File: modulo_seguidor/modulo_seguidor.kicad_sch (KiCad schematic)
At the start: 12 parts, among them J1 Battery, J4 Motor Izquierdo, J5 Motor Derecho, J6 puerto sensores, SW1 SW_Push, U1 LM7806_TO220

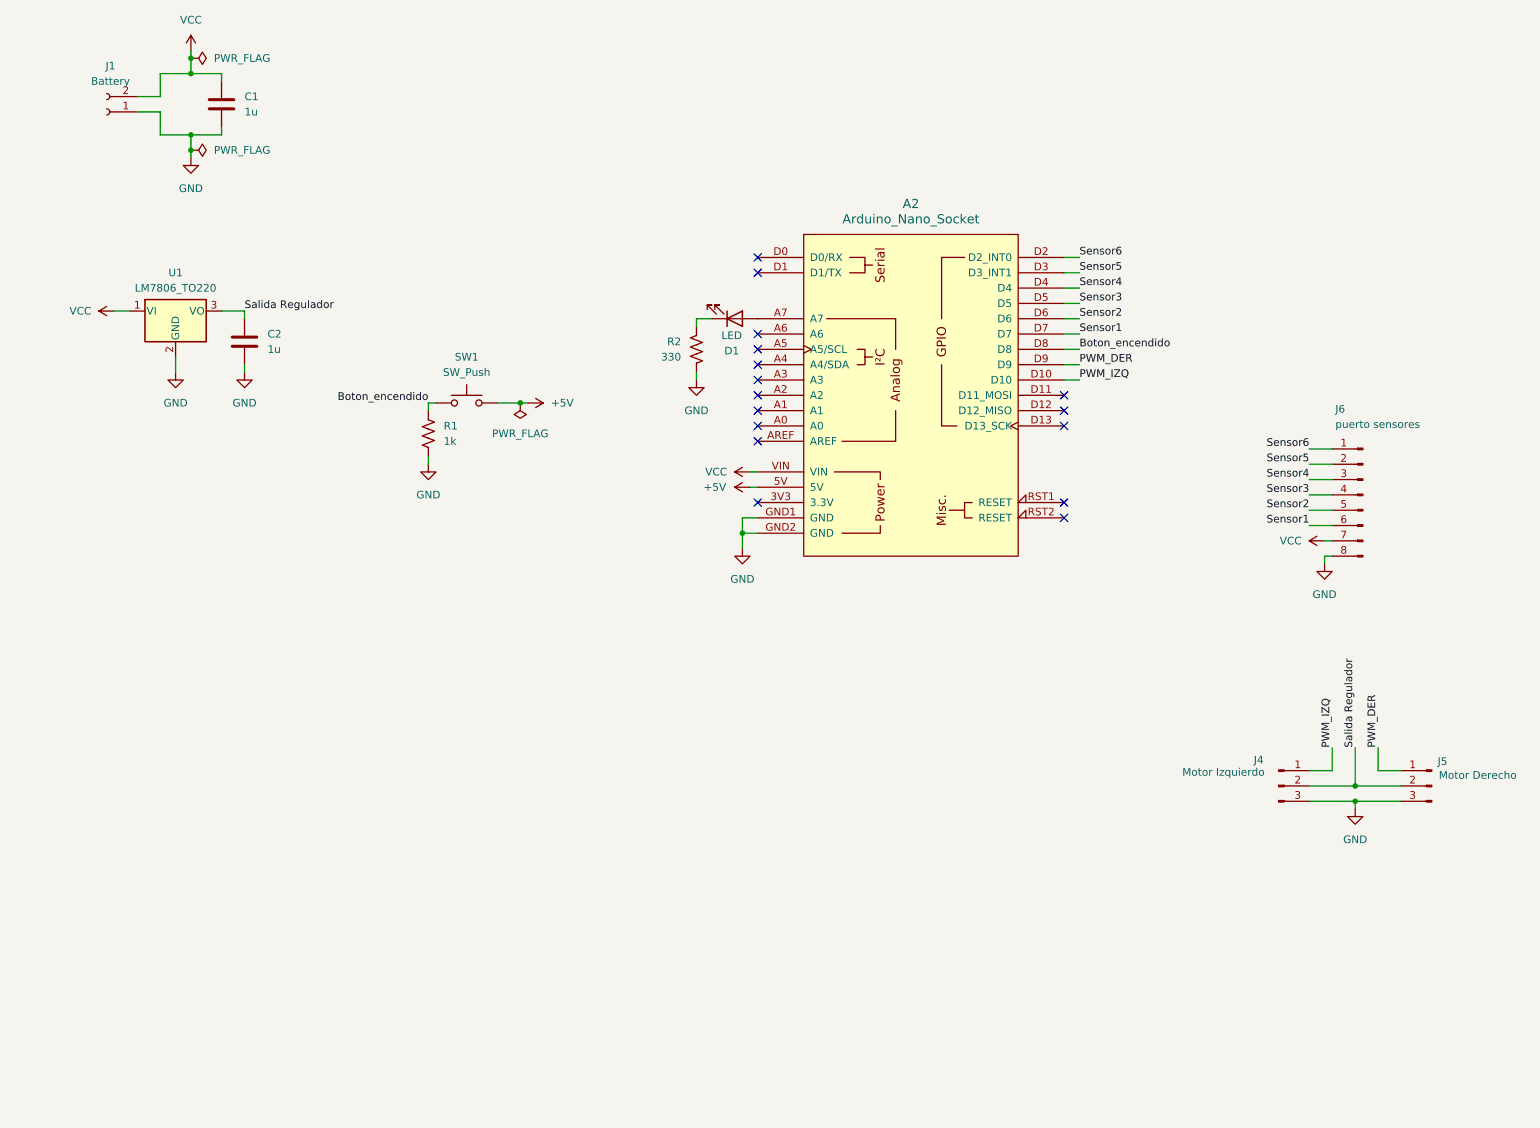
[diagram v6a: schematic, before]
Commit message: refactor(modulo_seguidor): Merge del seguidor y el puente H
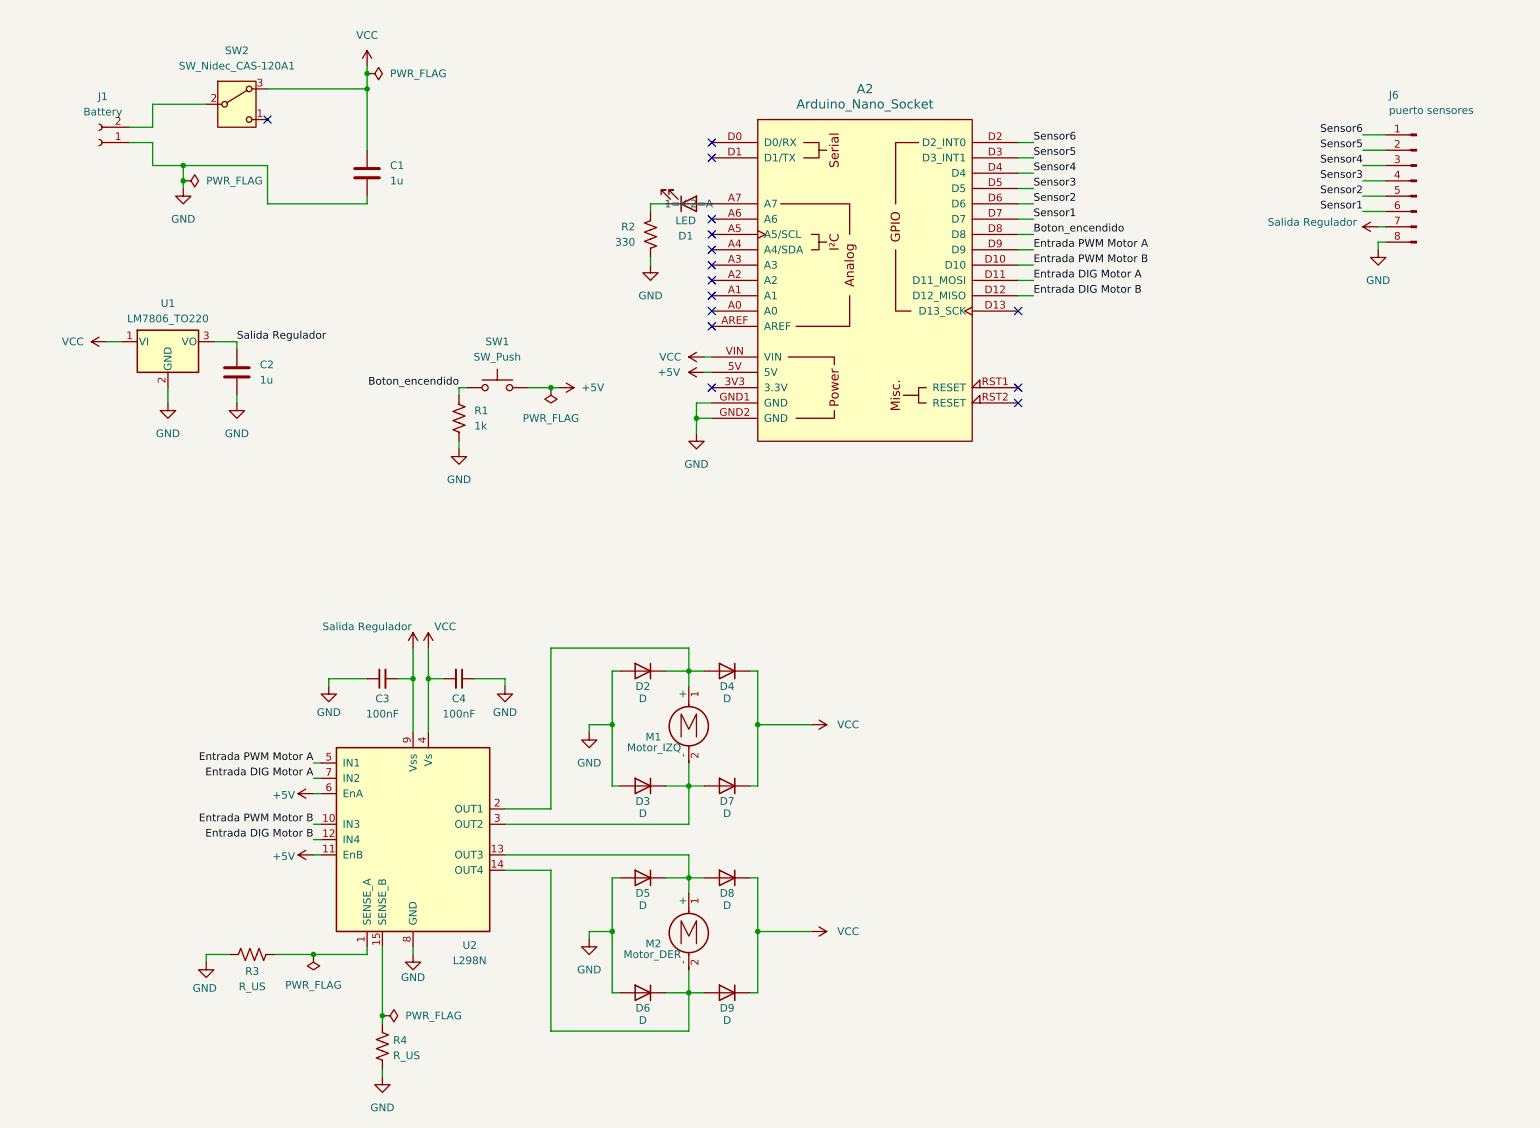
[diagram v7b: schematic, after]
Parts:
- removed J4: Motor Izquierdo, Connector_PinHeader_2.54mm:PinHeader_1x03_P2.54mm_Vertical, symbol Connector:Conn_01x03_Pin
- removed J5: Motor Derecho, Connector_PinHeader_2.54mm:PinHeader_1x03_P2.54mm_Vertical, symbol Connector:Conn_01x03_Pin
- added C3, C4: 100nF, Capacitor_THT:C_Disc_D7.0mm_W2.5mm_P5.00mm, symbol Device:C_Small
- added D2, D3, D4, D5, D6, D7, D8, D9: D, Diode_THT:D_DO-41_SOD81_P7.62mm_Horizontal, symbol Device:D
- added M1: Motor_IZQ, Resistor_THT:R_Axial_DIN0207_L6.3mm_D2.5mm_P2.54mm_Vertical, symbol Motor:Motor_DC
- added M2: Motor_DER, Resistor_THT:R_Axial_DIN0207_L6.3mm_D2.5mm_P2.54mm_Vertical, symbol Motor:Motor_DC
- added R3, R4: R_US, Resistor_SMD:R_0805_2012Metric_Pad1.20x1.40mm_HandSolder, symbol Device:R_US
- added SW2: SW_Nidec_CAS-120A1, Button_Switch_SMD:Nidec_Copal_CAS-120A, symbol Switch:SW_Nidec_CAS-120A1
- added U2: L298N, Package_TO_SOT_THT:TO-220-15_P2.54x5.08mm_StaggerOdd_Lead4.58mm_Vertical, symbol Driver_Motor:L298N
- A2: footprint PCM_arduino-library:Arduino_Nano_Socket -> Module:Arduino_Nano
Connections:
- net +5V: now also U2.11 (EnB), U2.6 (EnA)
- net GND: now also C3.1, C4.1, D2.2 (A), D3.2 (A), D5.2 (A), D6.2 (A), R3.2, R4.1, U2.8 (GND)
- net Salida Regulador: now also J6.7 (Pin_7), C3.2, U2.9 (Vss)
- net VCC: now also C4.2, D4.1 (K), D7.1 (K), D8.1 (K), D9.1 (K), SW2.3 (A), U2.4 (Vs); no longer J1.2 (Pin_2), J6.7 (Pin_7)
- net Entrada DIG Motor A: now reaches A2.D11 (D11_MOSI)
- net Entrada DIG Motor A: now also U2.7 (IN2)
- net Entrada DIG Motor B: now reaches A2.D12 (D12_MISO)
- net Entrada DIG Motor B: now also U2.12 (IN4)
- net PWM_DER renamed Entrada PWM Motor A
- net Entrada PWM Motor A: now also U2.5 (IN1)
- net PWM_IZQ renamed Entrada PWM Motor B
- net Entrada PWM Motor B: now also U2.10 (IN3)
- new net: R3.1, U2.1 (SENSE_A)
- new net: D3.1 (K), D7.2 (A), M1.2 (-), U2.3 (OUT2)
- new net: D5.1 (K), D8.2 (A), M2.1 (+), U2.13 (OUT3)
- new net: D6.1 (K), D9.2 (A), M2.2 (-), U2.14 (OUT4)
- new net: D2.1 (K), D4.2 (A), M1.1 (+), U2.2 (OUT1)
- new net: R4.2, U2.15 (SENSE_B)
- new net: J1.2 (Pin_2), SW2.2 (B)
- no-connect marks 16 -> 15
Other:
- moved on the sheet: A2, C1, C2, D1, J1, J6, R1, R2, SW1, U1

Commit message: feat(seguidor): Corrijo errores de DRC esquemático
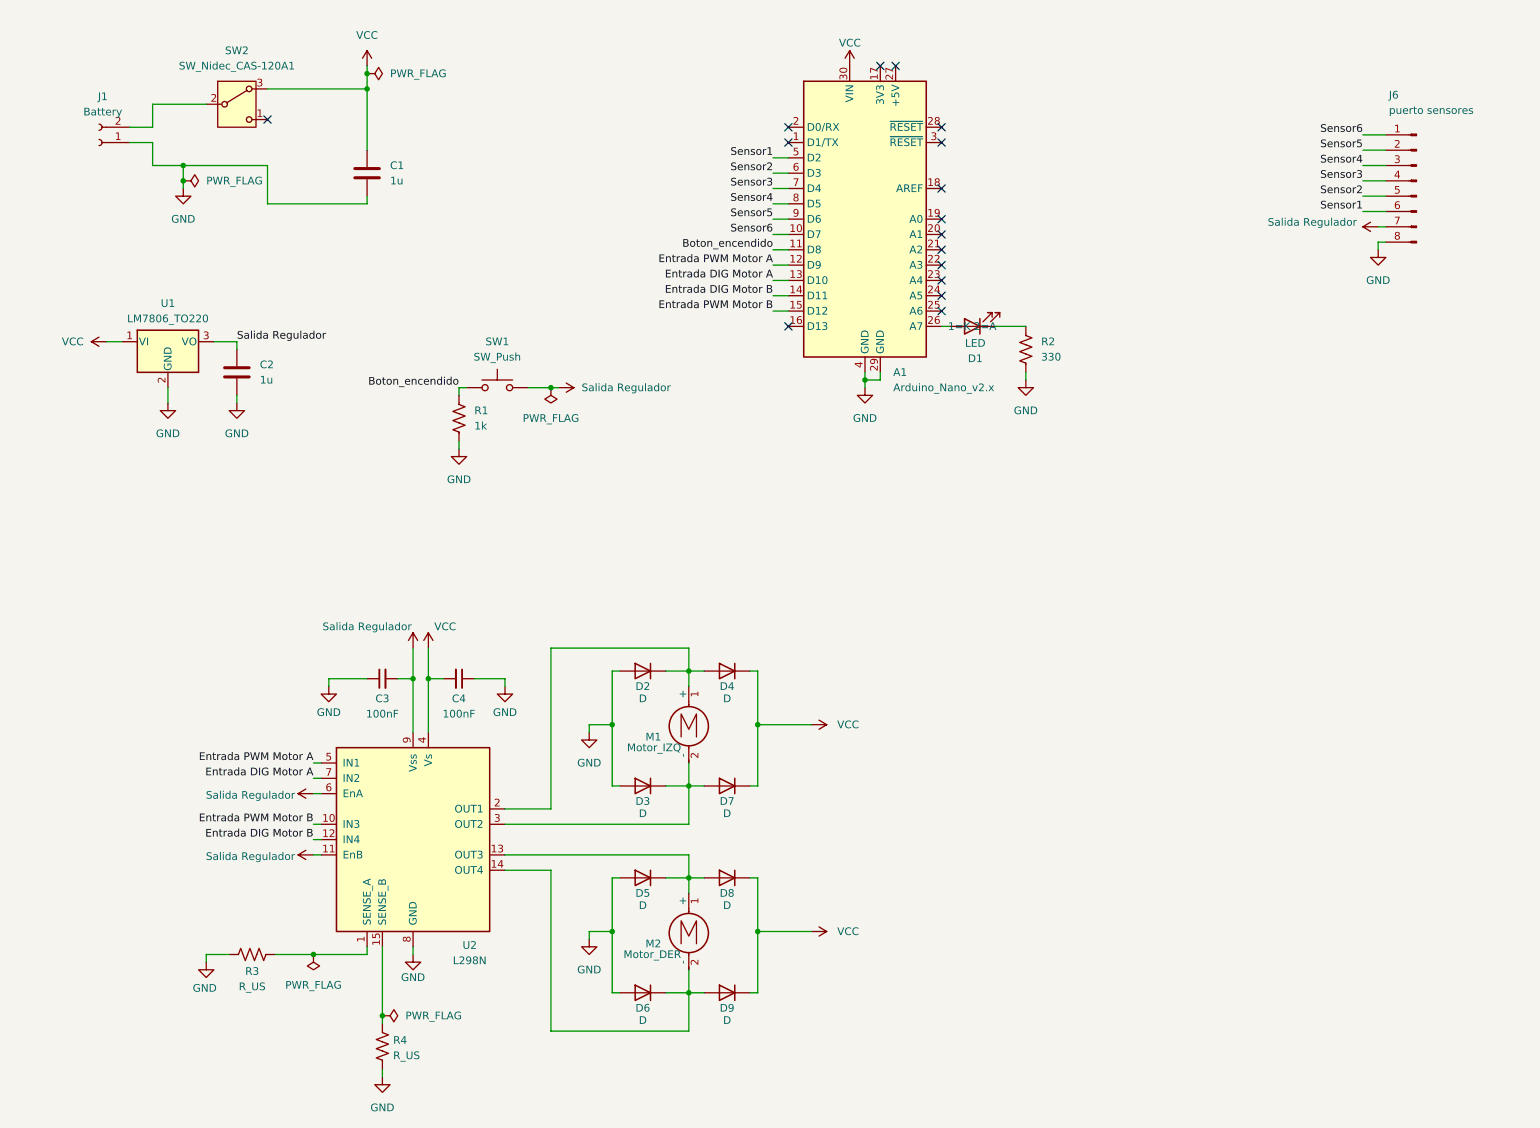
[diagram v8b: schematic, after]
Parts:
- removed A2: Arduino_Nano_Socket, Module:Arduino_Nano, symbol PCM_arduino-library:Arduino_Nano_Socket
- added A1: Arduino_Nano_v2.x, Module:Arduino_Nano, symbol MCU_Module:Arduino_Nano_v2.x
- SW2: footprint Button_Switch_SMD:Nidec_Copal_CAS-120A -> Converter_DCDC:Converter_DCDC_TRACO_TSR2-xxxx_THT
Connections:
- net +5V is gone; now on net Salida Regulador: SW1.1, U2.11 (EnB), U2.6 (EnA)
- net Boton_encendido: now also A1.11 (D8)
- net Entrada DIG Motor A: now also A1.13 (D10)
- net Entrada DIG Motor B: now also A1.14 (D11)
- net Entrada PWM Motor A: now also A1.12 (D9)
- net Entrada PWM Motor B: now also A1.15 (D12)
- net GND: now also A1.29 (GND), A1.4 (GND)
- net Sensor1: now also A1.5 (D2)
- net Sensor2: now also A1.6 (D3)
- net Sensor3: now also A1.7 (D4)
- net Sensor4: now also A1.8 (D5)
- net Sensor5: now also A1.9 (D6)
- net Sensor6: now also A1.10 (D7)
- net VCC: now also A1.30 (VIN)
- net at D1.2 (A): now also A1.26 (A7)
- no-connect marks 15 -> 16
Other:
- moved on the sheet: D1, R2
